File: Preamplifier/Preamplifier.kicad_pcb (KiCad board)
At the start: 2 copper layers, 70.1 x 55.2 mm, 90 parts, among them J1 Conn_01x02_Pin, J2 Conn_01x02_Pin, J3 Conn_01x02_Pin, J4 Conn_01x02_Pin, J5 Conn_01x03_Pin, U1 OPA1612AxD, U2 OPA1612AxD, U3 OPA1612AxD, U4 OPA1612AxD, U5 OPA1612AxD

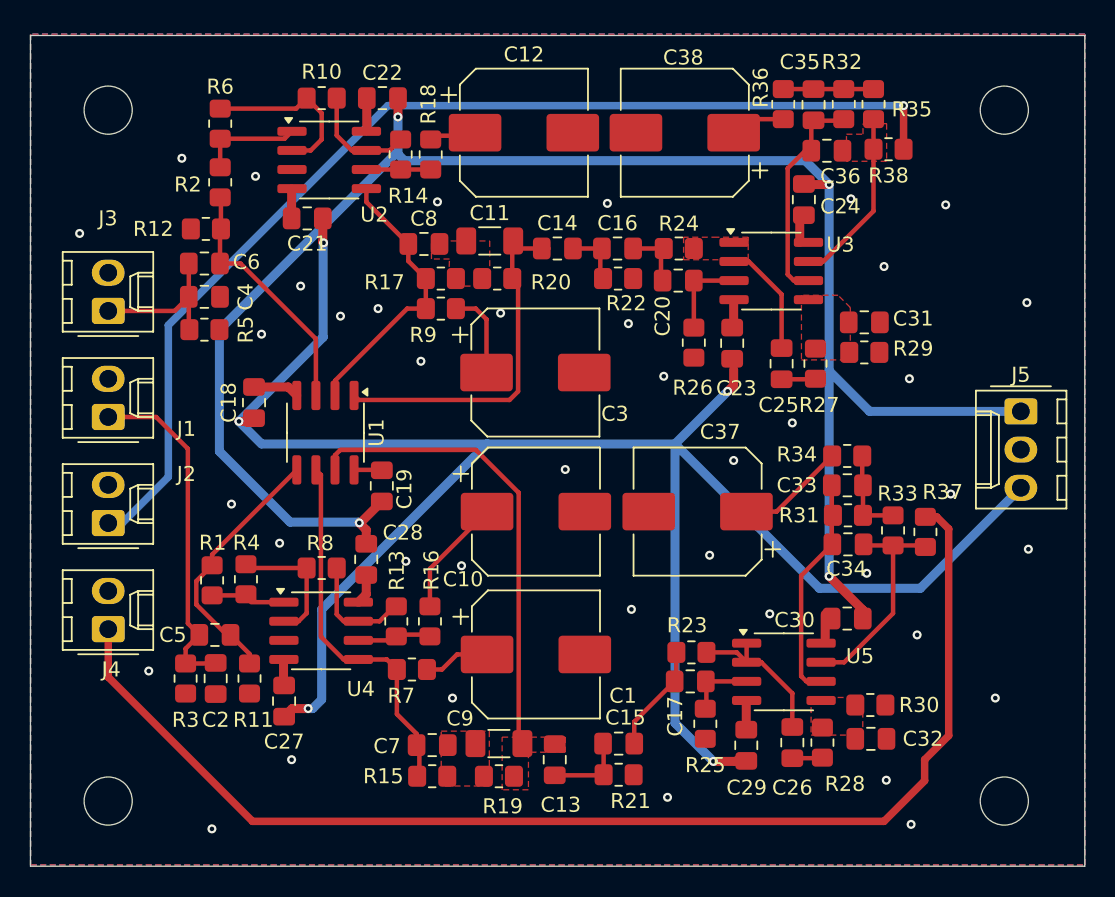
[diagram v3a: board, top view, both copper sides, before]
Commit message: READY FOR MANUFACTURING v3
preamplifier:
updated silkscreen
PS ready to manufacturing
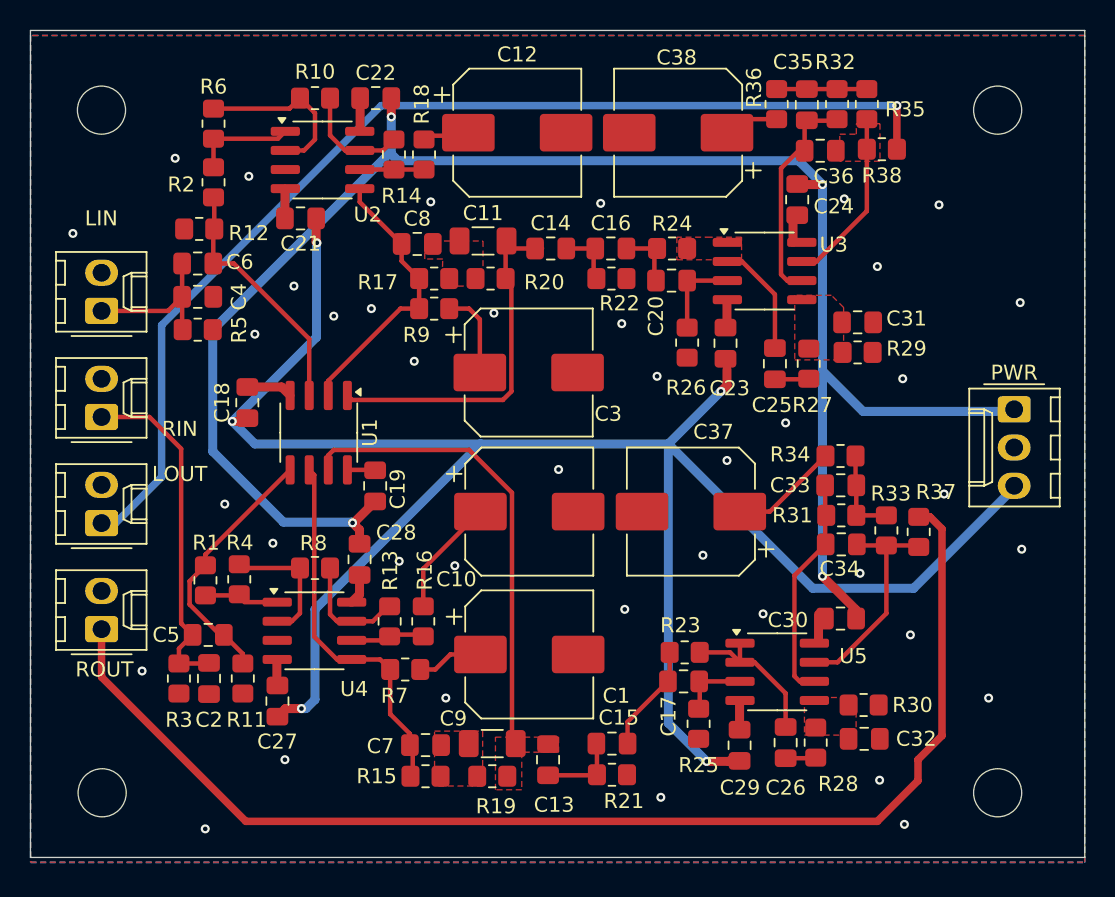
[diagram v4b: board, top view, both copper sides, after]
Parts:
- moved H2 0.71 mm to (164.5, 119.2)
- moved H4 0.68 mm to (104.9, 119.2)
- moved PWR 0.47 mm to (165.6, 93.7)
- moved C1 0.44 mm to (133.3, 110.0)
- moved C10 0.44 mm to (133.3, 100.5)
- moved C11 0.44 mm to (130.2, 82.5)
- moved C13 0.44 mm to (134.6, 117.0)
- moved C14 0.44 mm to (134.7, 83.0)
- moved C15 0.44 mm to (138.8, 115.9)
- moved C16 0.44 mm to (138.7, 83.0)
- moved C18 0.44 mm to (114.6, 93.2)
- moved C19 0.44 mm to (123.1, 98.8)
- moved C2 0.44 mm to (112.0, 111.6)
- moved C20 0.44 mm to (142.8, 85.1)
- moved C23 0.44 mm to (146.4, 89.3)
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- renumbered J3 to LIN, J2 to LOUT, J5 to PWR, J1 to RIN, J4 to ROUT
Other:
- board size 70.1 x 55.2 mm -> 70.1 x 55 mm

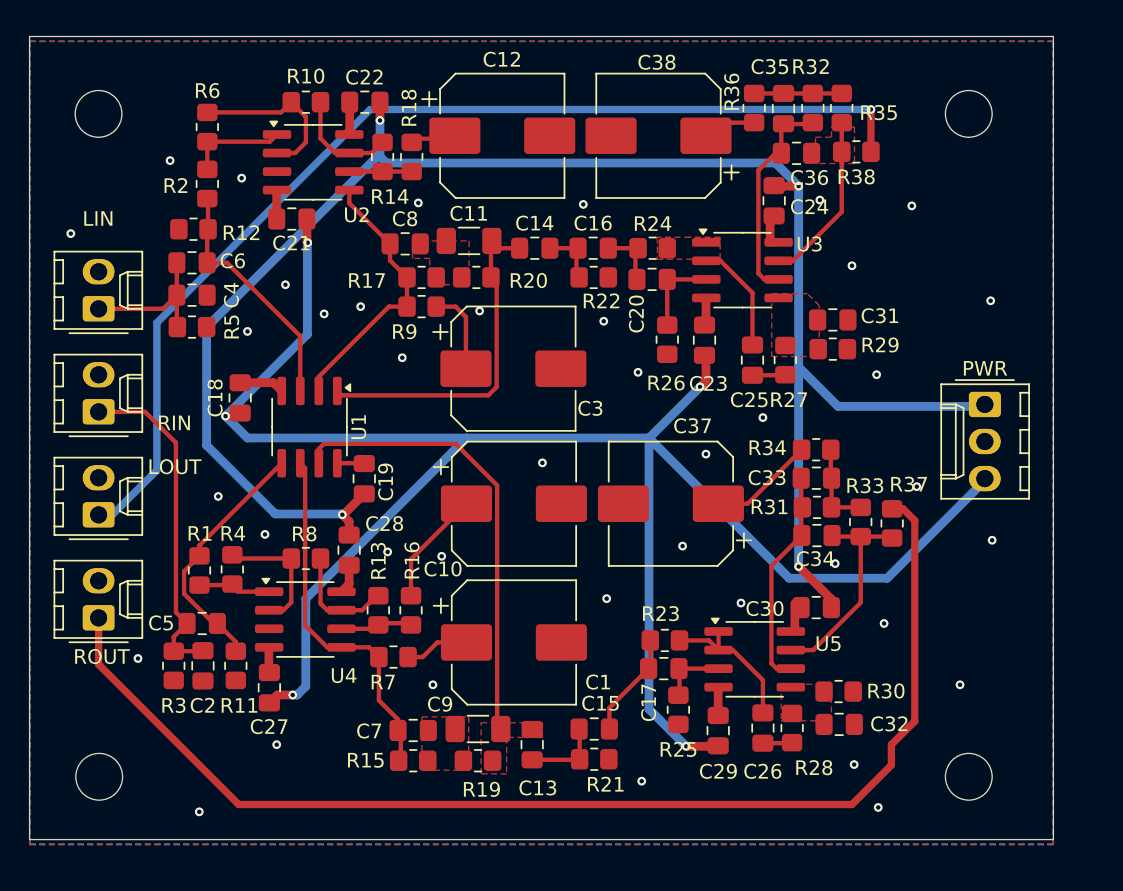
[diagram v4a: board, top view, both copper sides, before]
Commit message: Preamplifier Design
Updated the preamplifier board design.
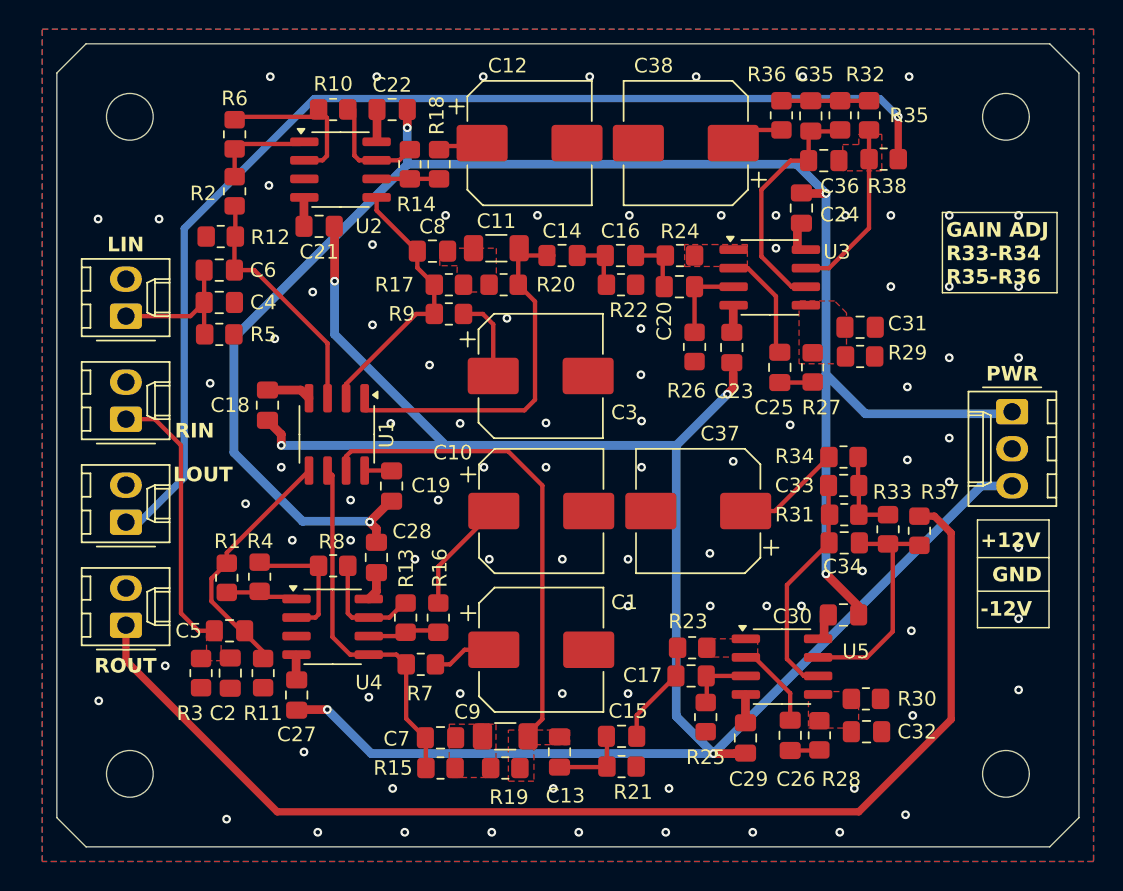
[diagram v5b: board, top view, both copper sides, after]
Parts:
- moved H2 2.55 mm to (167.0, 119.0)
- moved H3 2.55 mm to (167.0, 74.0)
- moved H1 2.15 mm to (107.0, 74.0)
- moved H4 2.11 mm to (107.0, 119.0)
- moved R16 1.93 mm to (128.1, 108.3)
- moved C1 1.93 mm to (135.2, 110.5)
- moved C10 1.93 mm to (135.2, 101.0)
- moved C11 1.93 mm to (132.1, 83.0)
- moved C12 1.93 mm to (134.4, 75.8)
- moved C13 1.93 mm to (136.4, 117.5)
- moved C14 1.93 mm to (136.6, 83.5)
- moved C15 1.93 mm to (140.7, 116.4)
- moved C16 1.93 mm to (140.6, 83.5)
- moved C17 1.93 mm to (145.4, 112.3)
- moved C18 1.93 mm to (116.4, 93.8)
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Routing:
- net Net-(J2-Pin_1): track 73.2 -> 78.3 mm
- net Net-(U5A--): track 10.4 -> 5.32 mm
- net Net-(J1-Pin_1): track 23.2 -> 18.8 mm
- net -12V: track 131.8 -> 135.7 mm
- net Net-(C13-Pad1): track 30.9 -> 32.8 mm
- net Net-(U3B--): track 14.3 -> 16.0 mm
- net Net-(C11-Pad2): track 22.8 -> 24.1 mm
- net Net-(C38-Pad1): track 3.72 -> 2.45 mm
- net Net-(U2A--): track 11.5 -> 10.6 mm
- net Net-(C34-Pad2): track 14.6 -> 15.4 mm
- net Net-(U4B--): track 4.97 -> 4.26 mm
- net Net-(R2-Pad2): track 6.88 -> 6.18 mm
- net Net-(U5B--): track 15.0 -> 15.7 mm
- net Net-(J4-Pin_1): track 81.9 -> 81.3 mm
- net Net-(R1-Pad2): track 4.95 -> 4.36 mm
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- added copper zone on F.Cu, net Net-(J1-Pin_1)
- added copper zone on F.Cu, net Net-(U5A--)
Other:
- board size 70.1 x 55 mm -> 70 x 55 mm
- board text added: "+12V"
- board text added: "-12V"
- board text added: "GAIN ADJ R33-R34 R35-R36"
- board text added: "GND"
- board text added: "PHONO PREAMP V1.0 REV.A PD 08/25"
